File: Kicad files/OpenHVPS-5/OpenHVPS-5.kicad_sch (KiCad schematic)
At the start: 81 parts, among them J1 Conn_01x03_Male, Q1 FQT7N10, Q2 BC846A, Q3 MMBT3906, Q4 MMBT3906, U1 MAX6008AEUR+T, U2 74HC14, U3 MAX4162, U4 CD14538BM

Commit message: Updated  with TP and some other small changes.
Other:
- moved on the sheet: C25, R23
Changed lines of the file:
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@@
     (stroke (width 0) (type solid) (color 0 0 0 0))
   )
-  (wire (pts (xy 19.685 165.735) (xy 19.685 159.385))
-    (stroke (width 0) (type solid) (color 0 0 0 0))
-  )
-  (wire (pts (xy 19.685 182.245) (xy 19.685 173.355))
+  (wire (pts (xy 19.685 168.275) (xy 19.685 159.385))
+    (stroke (width 0) (type solid) (color 0 0 0 0))
+  )
+  (wire (pts (xy 19.685 182.245) (xy 19.685 175.895))
     (stroke (width 0) (type solid) (color 0 0 0 0))
   )
@@
     (stroke (width 0) (type solid) (color 0 0 0 0))
   )
-  (wire (pts (xy 30.48 164.465) (xy 30.48 174.625))
+  (wire (pts (xy 30.48 164.465) (xy 30.48 168.275))
+    (stroke (width 0) (type solid) (color 0 0 0 0))
+  )
+  (wire (pts (xy 30.48 175.895) (xy 30.48 182.245))
     (stroke (width 0) (type solid) (color 0 0 0 0))
   )
   (wire (pts (xy 30.48 182.245) (xy 19.685 182.245))
+    (stroke (width 0) (type solid) (color 0 0 0 0))
+  )
+  (wire (pts (xy 30.48 182.245) (xy 30.48 185.42))
     (stroke (width 0) (type solid) (color 0 0 0 0))
   )
@@
     (pin "1")
   )
-  (symbol (lib_id "power:GND") (at 30.48 182.245 0) (unit 1)
-    (in_bom yes) (on_board yes)
-    (property "Reference" "#PWR02" (id 0) (at 30.48 188.595 0)
-      (effects (font (size 1.27 1.27)) hide)
-    )
-    (property "Value" "GND" (id 1) (at 30.607 186.6392 0))
-    (property "Footprint" "" (id 2) (at 30.48 182.245 0)
-      (effects (font (size 1.27 1.27)) hide)
-    )
-    (property "Datasheet" "" (id 3) (at 30.48 182.245 0)
+  (symbol (lib_id "power:GND") (at 30.48 185.42 0) (unit 1)
+    (in_bom yes) (on_board yes)
+    (property "Reference" "#PWR02" (id 0) (at 30.48 191.77 0)
+      (effects (font (size 1.27 1.27)) hide)
+    )
+    (property "Value" "GND" (id 1) (at 30.607 189.8142 0))
+    (property "Footprint" "" (id 2) (at 30.48 185.42 0)
+      (effects (font (size 1.27 1.27)) hide)
+    )
+    (property "Datasheet" "" (id 3) (at 30.48 185.42 0)
       (effects (font (size 1.27 1.27)) hide)
     )
@@
     (pin "2")
   )
-  (symbol (lib_id "Device:R") (at 30.48 178.435 0) (unit 1)
-    (in_bom yes) (on_board yes)
-    (property "Reference" "R23" (id 0) (at 32.258 177.267 0)
-      (effects (font (size 1.27 1.27)) (justify left))
-    )
-    (property "Value" "3.16M" (id 1) (at 32.258 179.578 0)
-      (effects (font (size 1.27 1.27)) (justify left))
-    )
-    (property "Footprint" "Resistor_SMD:R_0805_2012Metric" (id 2) (at 28.702 178.435 90)
-      (effects (font (size 1.27 1.27)) hide)
-    )
-    (property "Datasheet" "https://www.digikey.com/en/products/detail/yageo/RC0805FR-073M16L/727809" (id 3) (at 30.48 178.435 0)
+  (symbol (lib_id "Device:R") (at 30.48 172.085 0) (unit 1)
+    (in_bom yes) (on_board yes)
+    (property "Reference" "R23" (id 0) (at 32.893 170.282 0)
+      (effects (font (size 1.27 1.27)) (justify left))
+    )
+    (property "Value" "3.16M" (id 1) (at 32.258 173.228 0)
+      (effects (font (size 1.27 1.27)) (justify left))
+    )
+    (property "Footprint" "Resistor_SMD:R_0805_2012Metric" (id 2) (at 28.702 172.085 90)
+      (effects (font (size 1.27 1.27)) hide)
+    )
+    (property "Datasheet" "https://www.digikey.com/en/products/detail/yageo/RC0805FR-073M16L/727809" (id 3) (at 30.48 172.085 0)
       (effects (font (size 1.27 1.27)) hide)
     )
@@
     (pin "1")
   )
-  (symbol (lib_id "Device:C") (at 19.685 169.545 0) (unit 1)
-    (in_bom yes) (on_board yes)
-    (property "Reference" "C25" (id 0) (at 22.606 168.377 0)
-      (effects (font (size 1.27 1.27)) (justify left))
-    )
-    (property "Value" "1nF" (id 1) (at 22.606 170.688 0)
-      (effects (font (size 1.27 1.27)) (justify left))
-    )
-    (property "Footprint" "Capacitor_SMD:C_0805_2012Metric" (id 2) (at 20.65 173.355 0)
-      (effects (font (size 1.27 1.27)) hide)
-    )
-    (property "Datasheet" "https://www.digikey.com/en/products/detail/avx-corporation/08055C102KAT2A/563481" (id 3) (at 19.685 169.545 0)
-      (effects (font (size 1.27 1.27)) hide)
-    )
+  (symbol (lib_id "Device:C") (at 19.685 172.085 0) (unit 1)
+    (in_bom yes) (on_board yes)
+    (property "Reference" "C25" (id 0) (at 22.606 170.917 0)
+      (effects (font (size 1.27 1.27)) (justify left))
+    )
+    (property "Value" "1nF" (id 1) (at 22.606 173.228 0)
+      (effects (font (size 1.27 1.27)) (justify left))
+    )
+    (property "Footprint" "Capacitor_SMD:C_0805_2012Metric" (id 2) (at 20.65 175.895 0)
+      (effects (font (size 1.27 1.27)) hide)
+    )
+    (property "Datasheet" "https://www.digikey.com/en/products/detail/avx-corporation/08055C102KAT2A/563481" (id 3) (at 19.685 172.085 0)
+      (effects (font (size 1.27 1.27)) hide)
+    )

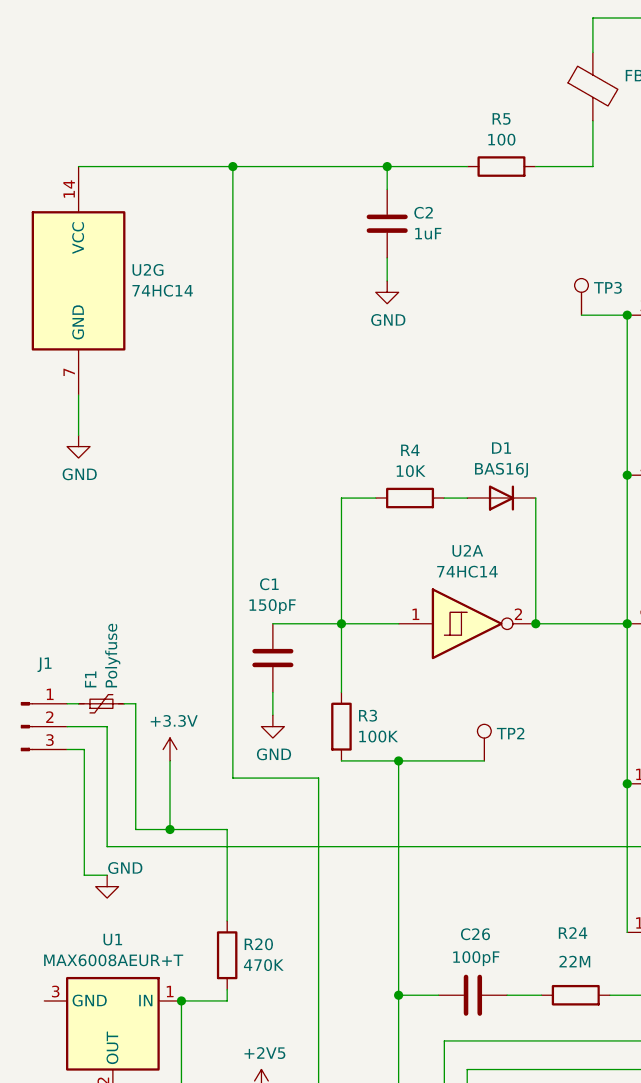
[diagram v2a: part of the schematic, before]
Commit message: Update text from SafePulse V1.1.2
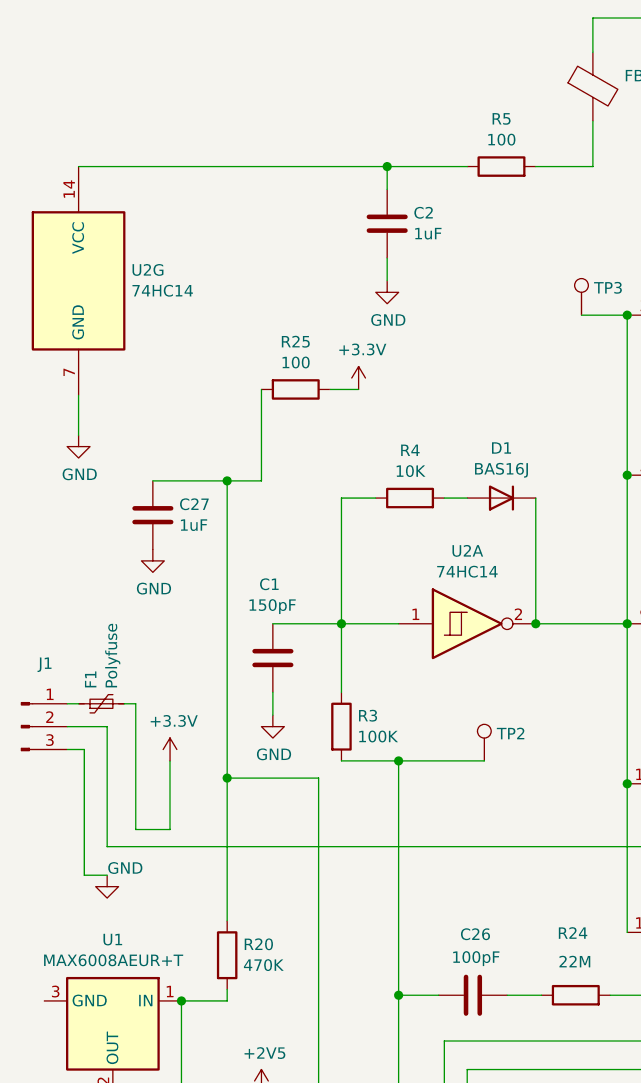
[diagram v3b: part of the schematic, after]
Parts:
- added C27: 1uF, Capacitor_SMD:C_0805_2012Metric, symbol Device:C
- added R25: 100, Resistor_SMD:R_0805_2012Metric, symbol Device:R
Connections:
- net +3V3: now also R25.1; no longer R20.1
- net GND: now also C27.2
- net at C2.1, R5.1, U2.14 (VCC): no longer U3.5 (V+)
- new net: C27.1, R20.1, R25.2, U3.5 (V+)
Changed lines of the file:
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@@
   (title_block
     (title "SafePulse")
-    (date "2021-02-18")
+    (date "2021-02-19")
     (rev "1.12")
     (company "SafeCast Team")
@@
   (junction (at 29.21 159.385) (diameter 1.016) (color 0 0 0 0))
   (junction (at 30.48 182.245) (diameter 1.016) (color 0 0 0 0))
-  (junction (at 34.29 111.125) (diameter 1.016) (color 0 0 0 0))
   (junction (at 35.56 130.175) (diameter 1.016) (color 0 0 0 0))
   (junction (at 35.56 140.335) (diameter 1.016) (color 0 0 0 0))
   (junction (at 35.56 159.385) (diameter 1.016) (color 0 0 0 0))
-  (junction (at 41.275 37.465) (diameter 1.016) (color 0 0 0 0))
+  (junction (at 40.64 72.39) (diameter 1.016) (color 0 0 0 0))
+  (junction (at 40.64 105.41) (diameter 1.016) (color 0 0 0 0))
   (junction (at 41.91 164.465) (diameter 1.016) (color 0 0 0 0))
   (junction (at 53.34 88.265) (diameter 1.016) (color 0 0 0 0))
@@
     (stroke (width 0) (type solid) (color 0 0 0 0))
   )
-  (wire (pts (xy 24.13 37.465) (xy 41.275 37.465))
+  (wire (pts (xy 24.13 37.465) (xy 58.42 37.465))
     (stroke (width 0) (type solid) (color 0 0 0 0))
   )
@@
     (stroke (width 0) (type solid) (color 0 0 0 0))
   )
+  (wire (pts (xy 32.385 72.39) (xy 40.64 72.39))
+    (stroke (width 0) (type solid) (color 0 0 0 0))
+  )
   (wire (pts (xy 34.29 103.505) (xy 34.29 111.125))
     (stroke (width 0) (type solid) (color 0 0 0 0))
   )
-  (wire (pts (xy 34.29 111.125) (xy 40.64 111.125))
-    (stroke (width 0) (type solid) (color 0 0 0 0))
-  )
   (wire (pts (xy 35.56 130.175) (xy 35.56 140.335))
     (stroke (width 0) (type solid) (color 0 0 0 0))
@@
     (stroke (width 0) (type solid) (color 0 0 0 0))
   )
-  (wire (pts (xy 40.64 111.125) (xy 40.64 121.285))
+  (wire (pts (xy 40.64 72.39) (xy 44.45 72.39))
+    (stroke (width 0) (type solid) (color 0 0 0 0))
+  )
+  (wire (pts (xy 40.64 105.41) (xy 40.64 72.39))
+    (stroke (width 0) (type solid) (color 0 0 0 0))
+  )
+  (wire (pts (xy 40.64 105.41) (xy 50.8 105.41))
+    (stroke (width 0) (type solid) (color 0 0 0 0))
+  )
+  (wire (pts (xy 40.64 121.285) (xy 40.64 105.41))
     (stroke (width 0) (type solid) (color 0 0 0 0))
   )
@@
     (stroke (width 0) (type solid) (color 0 0 0 0))
   )
-  (wire (pts (xy 41.275 37.465) (xy 58.42 37.465))
-    (stroke (width 0) (type solid) (color 0 0 0 0))
-  )
-  (wire (pts (xy 41.275 105.41) (xy 41.275 37.465))
-    (stroke (width 0) (type solid) (color 0 0 0 0))
-  )
   (wire (pts (xy 41.91 159.385) (xy 35.56 159.385))
     (stroke (width 0) (type solid) (color 0 0 0 0))
@@
     (stroke (width 0) (type solid) (color 0 0 0 0))
   )
+  (wire (pts (xy 44.45 72.39) (xy 44.45 62.23))
+    (stroke (width 0) (type solid) (color 0 0 0 0))
+  )
   (wire (pts (xy 44.45 140.335) (xy 35.56 140.335))
     (stroke (width 0) (type solid) (color 0 0 0 0))
@@
     (stroke (width 0) (type solid) (color 0 0 0 0))
   )
-  (wire (pts (xy 50.8 105.41) (xy 41.275 105.41))
-    (stroke (width 0) (type solid) (color 0 0 0 0))
-  )
   (wire (pts (xy 50.8 147.32) (xy 50.8 105.41))
+    (stroke (width 0) (type solid) (color 0 0 0 0))
+  )
+  (wire (pts (xy 52.07 62.23) (xy 55.245 62.23))
     (stroke (width 0) (type solid) (color 0 0 0 0))
   )
@@
     (pin "1")
   )
+  (symbol (lib_id "power:+3.3V") (at 55.245 62.23 0) (unit 1)
+    (in_bom yes) (on_board yes)
+    (property "Reference" "#PWR0102" (id 0) (at 55.245 66.04 0)
+      (effects (font (size 1.27 1.27)) hide)
+    )
+    (property "Value" "+3.3V" (id 1) (at 55.626 57.8358 0))
+    (property "Footprint" "" (id 2) (at 55.245 62.23 0)
+      (effects (font (size 1.27 1.27)) hide)
+    )
+    (property "Datasheet" "" (id 3) (at 55.245 62.23 0)
+      (effects (font (size 1.27 1.27)) hide)
+    )
+    (pin "1")
+  )
   (symbol (lib_id "power:+3.3V") (at 115.57 19.685 0) (unit 1)
     (in_bom yes) (on_board yes)
@@
     (pin "1")
   )
+  (symbol (lib_id "power:GND") (at 32.385 80.01 0) (unit 1)
+    (in_bom yes) (on_board yes)
+    (property "Reference" "#PWR0101" (id 0) (at 32.385 86.36 0)
+      (effects (font (size 1.27 1.27)) hide)
+    )
+    (property "Value" "GND" (id 1) (at 32.512 84.4042 0))
+    (property "Footprint" "" (id 2) (at 32.385 80.01 0)
+      (effects (font (size 1.27 1.27)) hide)
+    )
+    (property "Datasheet" "" (id 3) (at 32.385 80.01 0)
+      (effects (font (size 1.27 1.27)) hide)
+    )
+    (pin "1")
+  )
   (symbol (lib_id "power:GND") (at 45.72 98.425 0) (unit 1)
     (in_bom yes) (on_board yes)
@@
     )
     (property "Datasheet" "https://www.digikey.com/en/products/detail/te-connectivity-passive-product/CRG0805F470K/2380908" (id 3) (at 40.64 125.095 0)
+      (effects (font (size 1.27 1.27)) hide)
+    )
+    (pin "1")
+    (pin "2")
+  )
+  (symbol (lib_id "Device:R") (at 48.26 62.23 270) (unit 1)
+    (in_bom yes) (on_board yes)
+    (property "Reference" "R25" (id 0) (at 48.26 56.972 90))
+    (property "Value" "100" (id 1) (at 48.26 59.2836 90))
+    (property "Footprint" "Resistor_SMD:R_0805_2012Metric" (id 2) (at 48.26 60.452 90)
+      (effects (font (size 1.27 1.27)) hide)
+    )
+    (property "Datasheet" "https://www.digikey.com/en/products/detail/te-connectivity-passive-product/CRG0805F100R/2380830" (id 3) (at 48.26 62.23 0)
       (effects (font (size 1.27 1.27)) hide)
     )
@@
     )
     (property "Datasheet" "https://www.digikey.com/en/products/detail/avx-corporation/08055C102KAT2A/563481" (id 3) (at 19.685 172.085 0)
+      (effects (font (size 1.27 1.27)) hide)
+    )
+    (pin "1")
+    (pin "2")
+  )
+  (symbol (lib_id "Device:C") (at 32.385 76.2 0) (unit 1)
+    (in_bom yes) (on_board yes)
+    (property "Reference" "C27" (id 0) (at 35.306 75.032 0)
+      (effects (font (size 1.27 1.27)) (justify left))
+    )
+    (property "Value" "1uF" (id 1) (at 35.306 77.343 0)
+      (effects (font (size 1.27 1.27)) (justify left))
+    )
+    (property "Footprint" "Capacitor_SMD:C_0805_2012Metric" (id 2) (at 33.35 80.01 0)
+      (effects (font (size 1.27 1.27)) hide)
+    )
+    (property "Datasheet" "https://www.digikey.com/en/products/detail/samsung-electro-mechanics/CL21B105KOFNNNG/3894469" (id 3) (at 32.385 76.2 0)
       (effects (font (size 1.27 1.27)) hide)
     )
@@
       (reference "#PWR025") (unit 1) (value "GND") (footprint "")
     )
+    (path "/b8ee2644-becf-4fe4-a3c0-41197f03a0e1"
+      (reference "#PWR0101") (unit 1) (value "GND") (footprint "")
+    )
+    (path "/340a57e5-1fe0-423e-825b-82a403d4e016"
+      (reference "#PWR0102") (unit 1) (value "+3.3V") (footprint "")
+    )
     (path "/00000000-0000-0000-0000-0000600fa622"
       (reference "C1") (unit 1) (value "150pF") (footprint "Capacitor_SMD:C_0805_2012Metric")
@@
       (reference "C26") (unit 1) (value "100pF") (footprint "Capacitor_SMD:C_0805_2012Metric")
     )
+    (path "/3d3074de-d2e4-412b-bf2b-8e6e9452992f"
+      (reference "C27") (unit 1) (value "1uF") (footprint "Capacitor_SMD:C_0805_2012Metric")
+    )
     (path "/00000000-0000-0000-0000-0000600ddc6a"
       (reference "D1") (unit 1) (value "BAS16J") (footprint "Diode_SMD:D_SOD-323")
@@
       (reference "R24") (unit 1) (value "22M") (footprint "Resistor_SMD:R_0805_2012Metric")
     )
+    (path "/6262f35d-33c6-4702-969c-2648bf6ad569"
+      (reference "R25") (unit 1) (value "100") (footprint "Resistor_SMD:R_0805_2012Metric")
+    )
     (path "/a00aaed8-a3fc-4d63-a7e6-25589e061b4e"

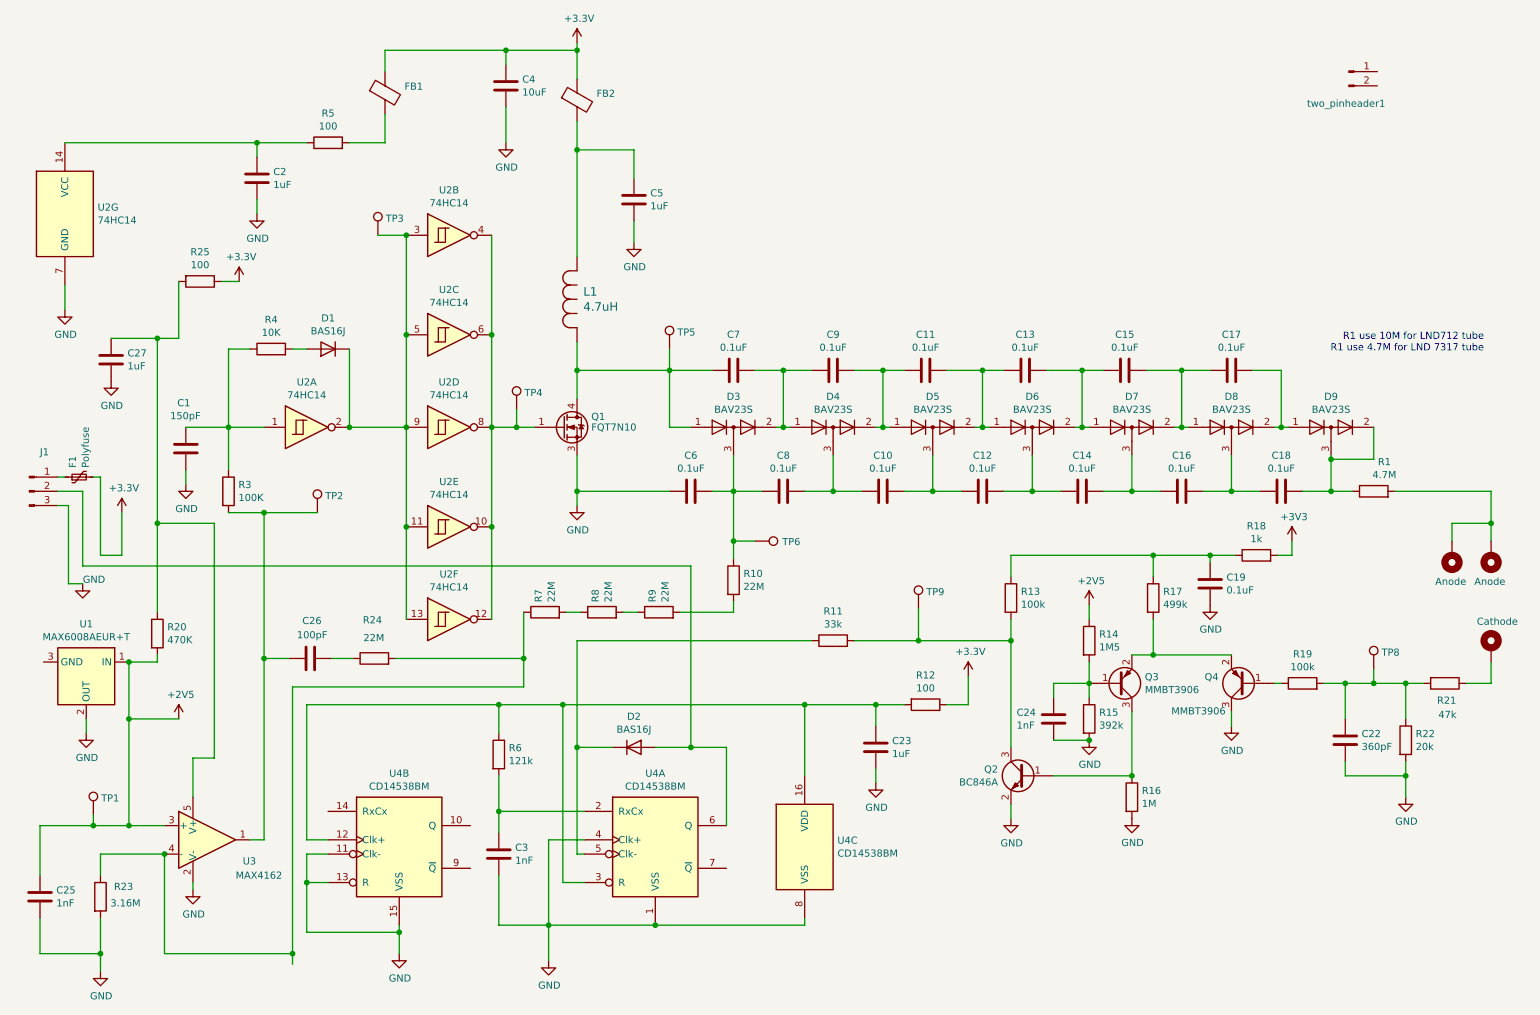
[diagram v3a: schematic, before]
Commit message: Chnaged R4 and C1 label placement
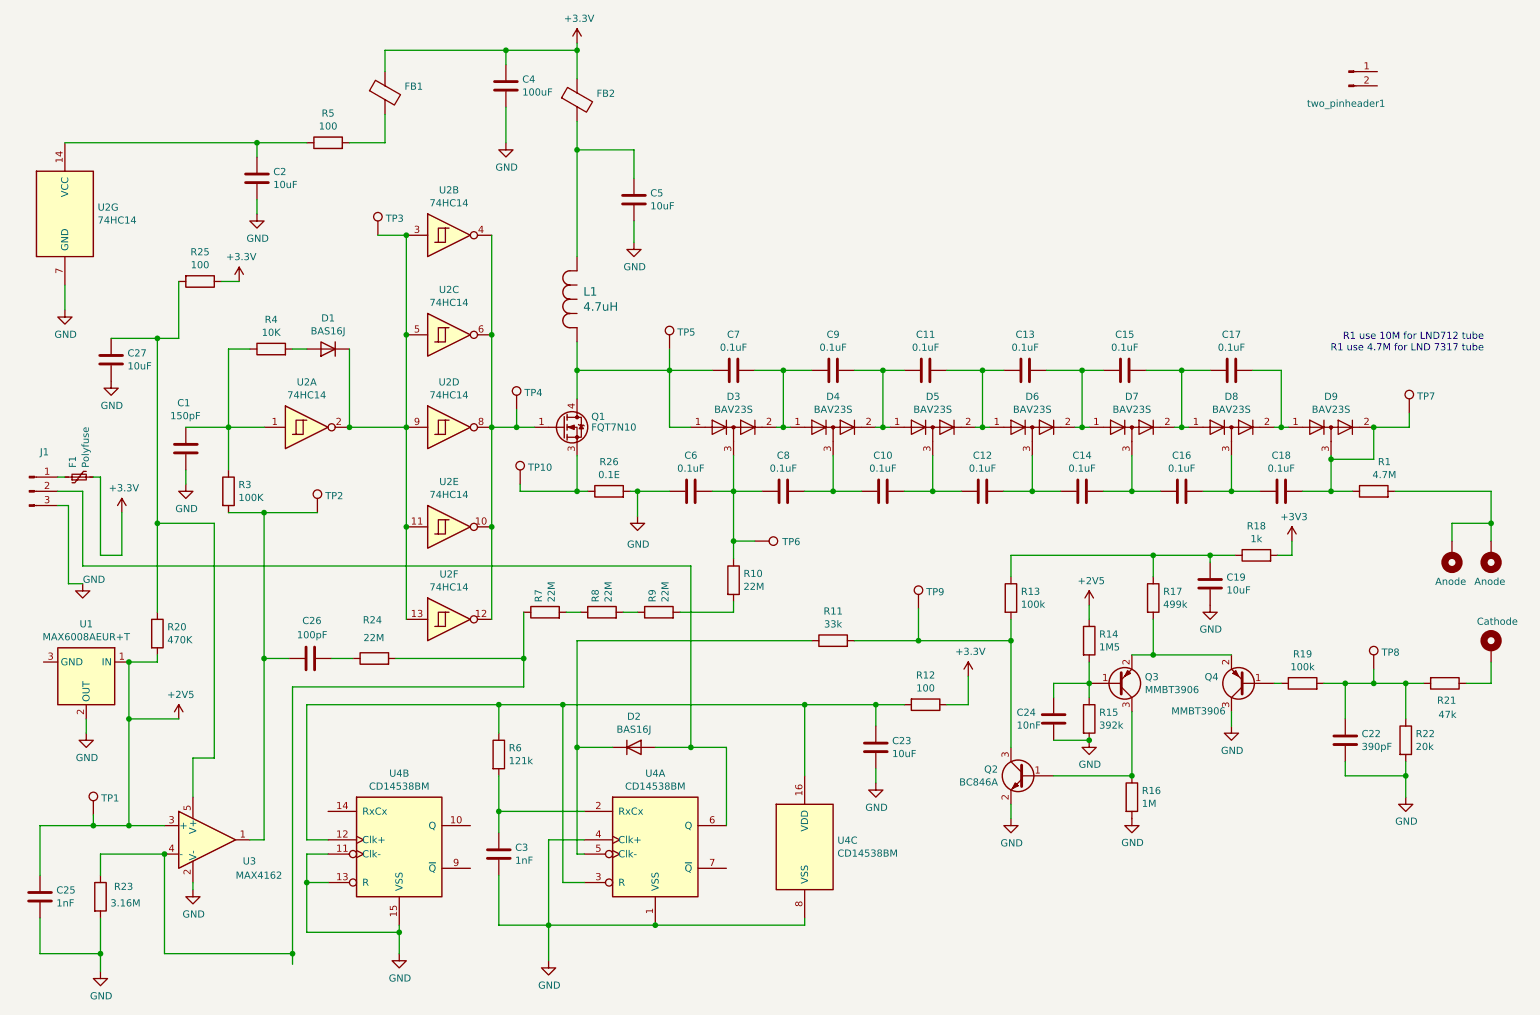
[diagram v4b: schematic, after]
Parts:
- added R26: 0.1E, Resistor_SMD:R_0805_2012Metric, symbol Device:R
- added TP10, TP7: TestPoint, TestPoint:TestPoint_Pad_1.0x1.0mm, symbol Connector:TestPoint
- C19: value 0.1uF -> 10uF
- C2, C23, C27, C5: value 1uF -> 10uF
- C22: value 360pF -> 390pF
- C24: value 1nF -> 10nF
- C4: value 10uF -> 100uF
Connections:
- net GND: now also R26.2; no longer Q1.3 (S)
- net at C18.2, D9.2 (A), D9.3 (K)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: now also TP7.1
- new net: Q1.3 (S), R26.1, TP10.1
